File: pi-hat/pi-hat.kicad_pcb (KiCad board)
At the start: 2 copper layers, 65 x 56 mm, 67 parts, among them J1 Conn_01x04_Male, J2 Conn_01x04_Male, J3 Conn_01x05_Male, J4 Conn_01x05_Male, J5 Conn_01x05_Male, J6 Conn_01x05_Male, J7 Conn_01x07_Male, J8 Conn_01x07_Male, P1 Conn_02x20_Odd_Even, Q1 BSS138, Q10 AO 3415A, Q11 AO 3415A, Q12 BSS138, Q13 BSS138, Q14 BSS138, Q15 BSS138, Q16 BSS138, Q2 BSS138, Q3 BSS138, Q4 BC 807-25, Q5 AO 3415A, Q6 BC 807-25, Q7 BC 818-25, Q8 BC 818-25, Q9 BC 818-25, U1 M24C02-WMN

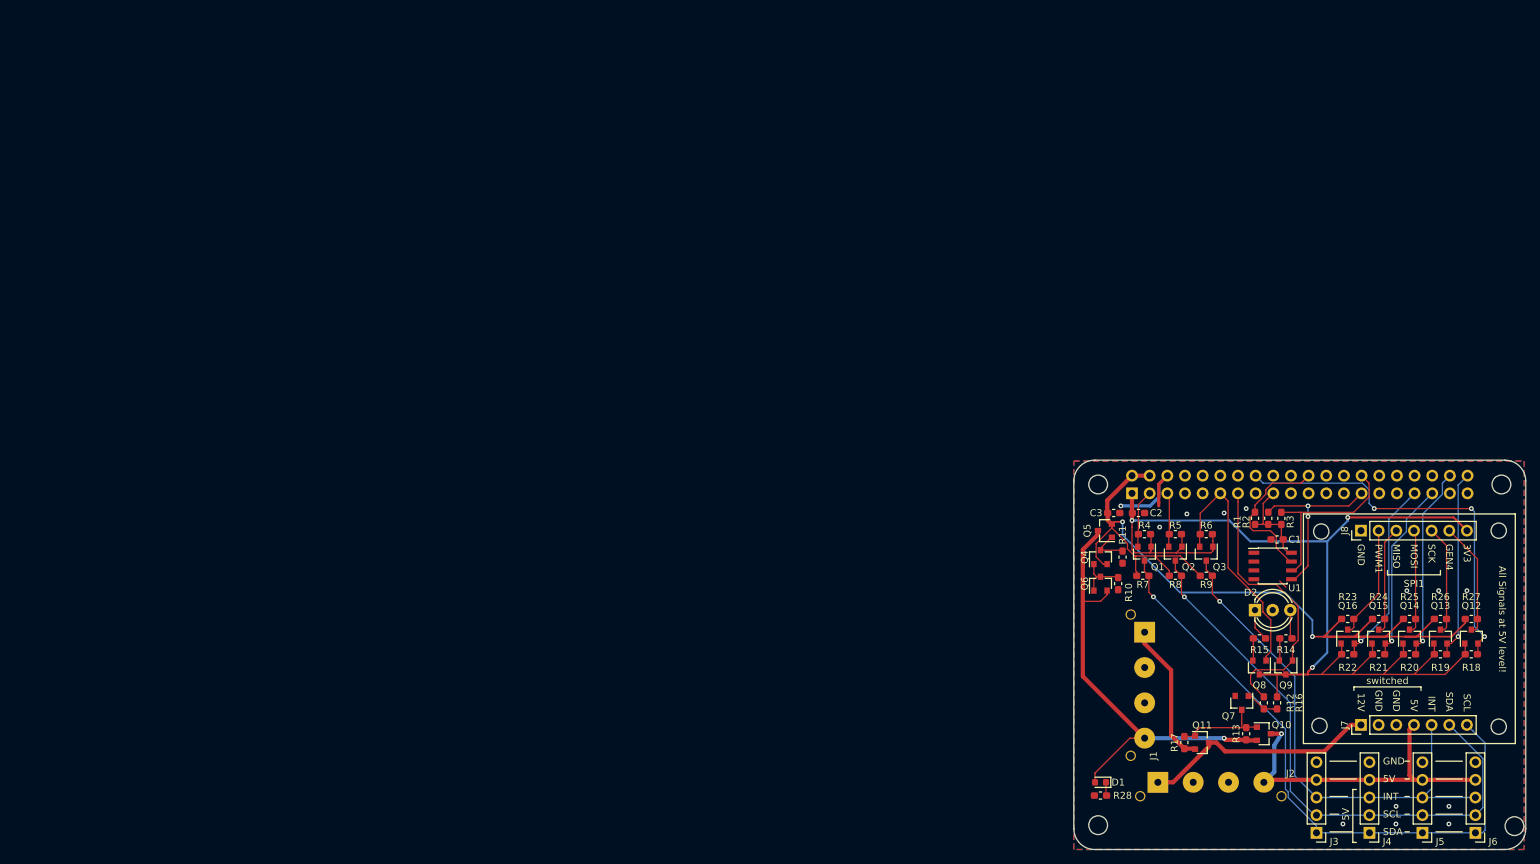
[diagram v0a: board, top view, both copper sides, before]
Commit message: PiHat: 2nd revision
* Checked and adapted MOSFET high-side switches
* remove J6 for space and fix mounting hole
* Fix Molex connectors
* Capacitors
* Extension board positions
* General layout
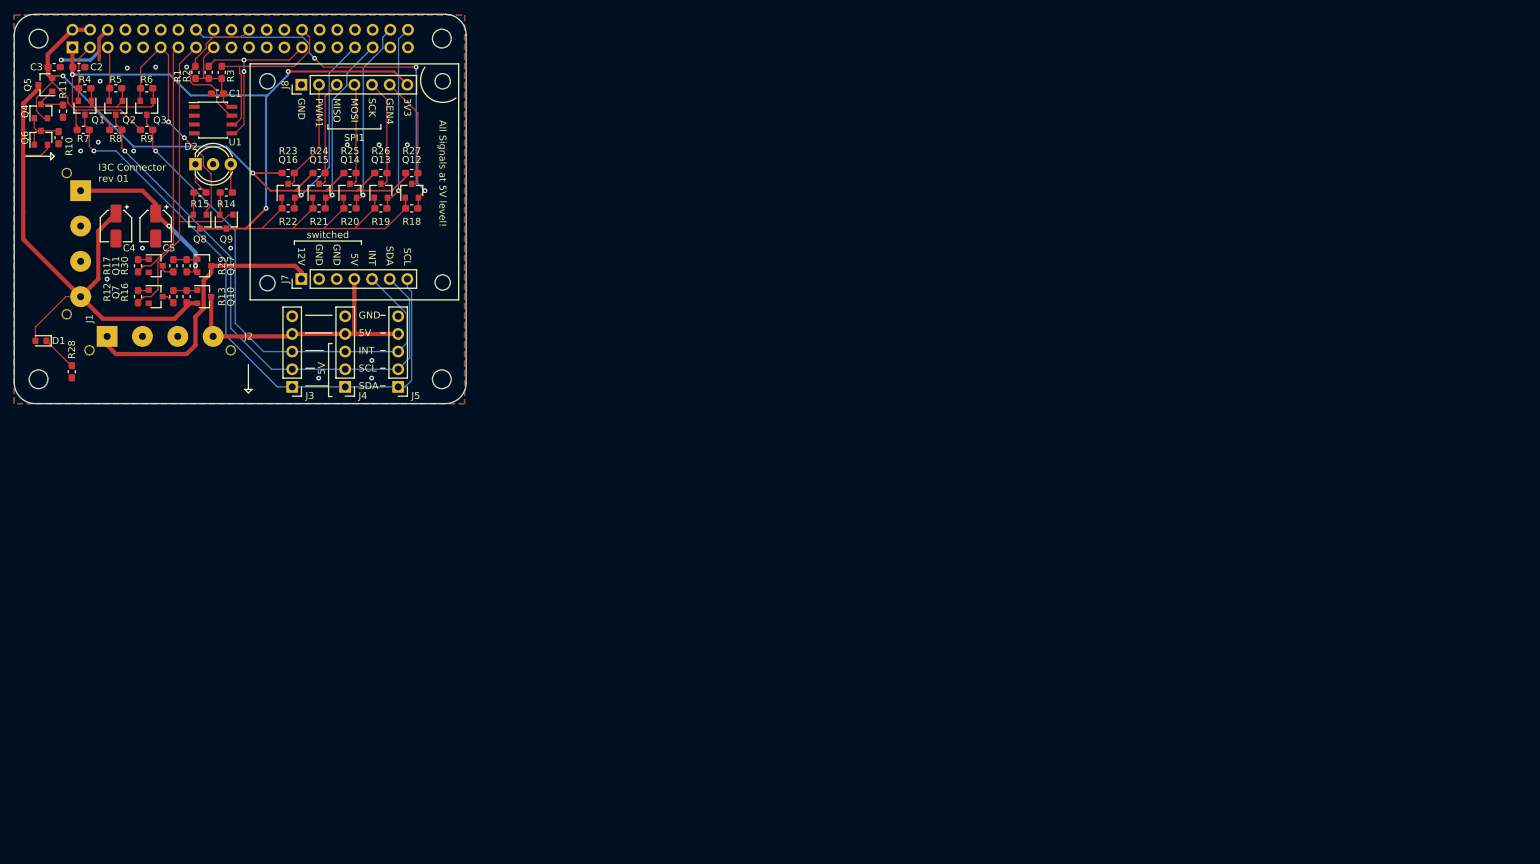
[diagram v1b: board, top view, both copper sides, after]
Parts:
- removed J6: Conn_01x05_Male, Connector_PinHeader_2.54mm:PinHeader_1x05_P2.54mm_Vertical
- added C4: 47u, Capacitor_SMD:CP_Elec_4x4.5, F.Cu at (62.2, 60.3)
- added C5: 47u, Capacitor_SMD:CP_Elec_4x4.5, F.Cu at (67.9, 60.3)
- added Q17: AO 3415A, Package_TO_SOT_SMD:SOT-23, F.Cu at (74.9, 66.0)
- added R29: 1K, Capacitor_SMD:C_0603_1608Metric_Pad1.05x0.95mm_HandSolder, F.Cu at (72.4, 66.0)
- added R30: 10R, Capacitor_SMD:C_0603_1608Metric_Pad1.05x0.95mm_HandSolder, F.Cu at (70.5, 66.0)
- Q11: value AO 3415A -> BC 818-25
- R12: value 330R -> 220R
- R16: value 1K -> 10R
- R17: value 1K -> 220R
- moved R12 172.1 mm to (65.4, 70.5), turned to 270 degrees
- moved R16 169.2 mm to (70.5, 70.5)
- moved MK4 167.1 mm to (109.1, 82.5)
- moved Q7 166.8 mm to (67.9, 70.5), turned to 0 degrees
- moved J1 165.7 mm to (57.1, 62.9)
- moved Q11 165.4 mm to (67.9, 66.0)
- moved R17 165.4 mm to (65.4, 66.0), turned to 270 degrees
- moved C1 165.3 mm to (76.8, 41.3)
- moved C3 165.3 mm to (53.3, 37.5)
- moved D2 165.3 mm to (73.7, 51.4)
- moved J7 165.3 mm to (88.9, 67.9)
- moved J8 165.3 mm to (88.9, 40.0)
- moved MK1 165.3 mm to (51.1, 33.4)
- moved MK2 165.3 mm to (109.1, 33.4)
- moved MK3 165.3 mm to (51.1, 82.4)
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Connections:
- P1 pad 13: ACTIVATE -> ACTIVATE_12V
- P1 pad 15: (no net) -> ACTIVATE_5V
- Q11 pad 1: Net-(Q10-Pad1) -> Net-(Q11-Pad1)
- Q11 pad 2: +12V -> GND
- Q11 pad 3: +12VA -> Net-(Q11-Pad3)
- Q7 pad 3: Net-(Q10-Pad1) -> Net-(Q7-Pad3)
- Q9 pad 1: ACTIVATE -> ACTIVATE_5V
- R12 pad 2: ACTIVATE -> ACTIVATE_5V
- R16 pad 1: +3V3 -> Net-(Q10-Pad1)
- R16 pad 2: Net-(Q7-Pad1) -> Net-(Q7-Pad3)
- R17 pad 1: +12V -> Net-(Q11-Pad1)
- R17 pad 2: Net-(Q10-Pad1) -> ACTIVATE_12V
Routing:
- net ACTIVATE_5V: track 0.00 -> 48.9 mm
- net ACTIVATE: track 41.2 -> 0.00 mm
- net ACTIVATE_12V: track 0.00 -> 35.3 mm
- net +5VP: track 65.7 -> 85.2 mm, vias 1 -> 0
- net +5V: track 128.6 -> 116.4 mm
- net Net-(Q10-Pad1): track 13.9 -> 3.48 mm
- net +12VA: track 34.0 -> 41.7 mm
- net +5VA: track 48.4 -> 41.7 mm, vias 1 -> 0
- net +12V: track 20.7 -> 27.2 mm, vias 0 -> 2
- net SCL_5V: track 83.5 -> 79.2 mm
- net Net-(Q17-Pad1): track 0.00 -> 3.48 mm
- net Net-(Q7-Pad1): track 4.91 -> 1.57 mm
- net Net-(D1-Pad1): track 1.94 -> 5.14 mm
- net +3V3: track 159.9 -> 156.9 mm
- net SDA_5V: track 90.0 -> 87.0 mm
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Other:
- board text added: "I3C Connector rev 01"
- board text added: "RASPBERRY-PI 40-PIN ADDON BOARD VIEW FROM TOP NOTE: P1 SHOULD BE FITTED ON THE REVERSE OF THE BOARD"
- board text removed: "RASPBERRY-PI 40-PIN ADDON BOARD VIEW FROM TOP NOTE: P1 SHOULD BE FITTED ON THE REVERSE OF THE BOARD ADD EDGE CUTS FROM CAMERA AND DISPLAY PORTS AS REQUIRED"

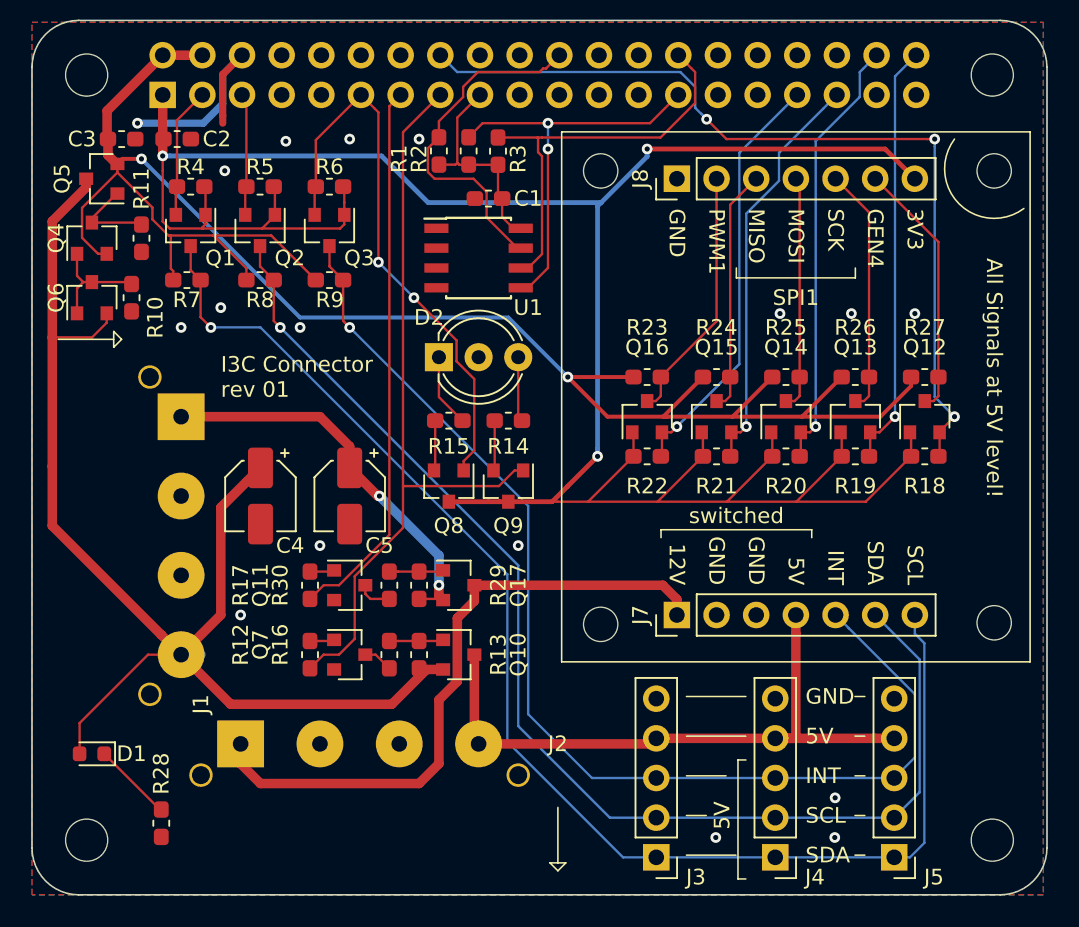
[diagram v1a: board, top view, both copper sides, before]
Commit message: Final fixes
* make sheet bigger (A3) to fix everything nicely
* fix INT LED to be low active
* fix molex holes
* fix base resistors
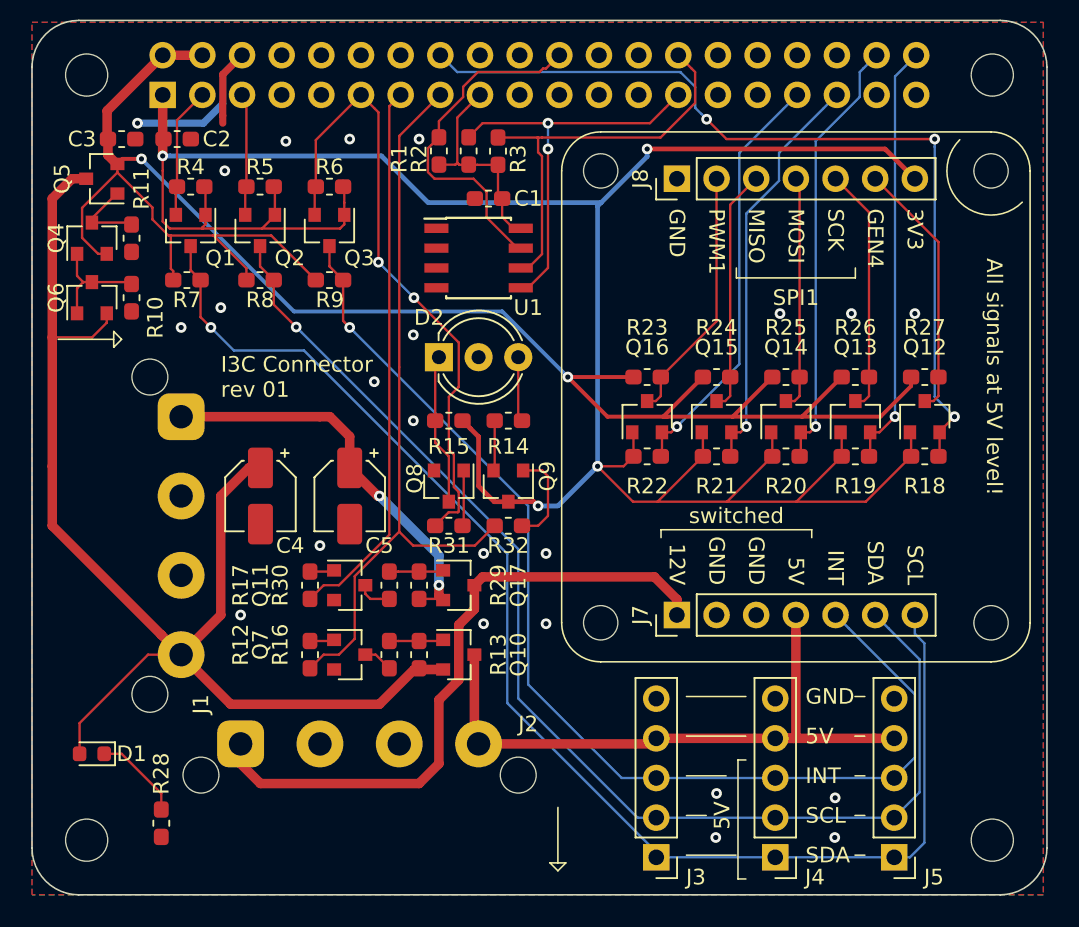
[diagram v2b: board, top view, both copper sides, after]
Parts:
- added R31: 330R, Capacitor_SMD:C_0603_1608Metric_Pad1.05x0.95mm_HandSolder, F.Cu at (74.3, 62.2)
- added R32: 330R, Capacitor_SMD:C_0603_1608Metric_Pad1.05x0.95mm_HandSolder, F.Cu at (78.1, 62.2)
- R12, R17: value 220R -> 330R
- R13, R29: value 1K -> 100K
- moved R11 0.63 mm to (54.0, 43.8)
- moved MK7 0.20 mm to (109.0, 39.5)
- moved MK8 0.20 mm to (109.0, 68.4)
- moved MK6 0.10 mm to (84.0, 68.4)
- turned R15 to 180 degrees
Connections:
- Q8 pad 1: INT -> Net-(Q8-Pad1)
- Q8 pad 2: Net-(Q8-Pad2) -> GND
- Q8 pad 3: +3V3 -> Net-(D2-Pad1)
- Q9 pad 1: ACTIVATE_5V -> Net-(Q9-Pad1)
- R15 pad 1: Net-(Q8-Pad2) -> +3V3
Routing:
- net Net-(Q9-Pad1): track 0.00 -> 6.21 mm
- net Net-(D2-Pad1): track 4.69 -> 9.72 mm
- net INT: track 36.3 -> 40.6 mm
- net Net-(Q8-Pad1): track 0.00 -> 3.57 mm
- net Net-(Q8-Pad2): track 3.22 -> 0.00 mm
- net +12V: track 27.2 -> 25.9 mm
- net INT_5V: track 73.5 -> 72.4 mm
- net ACTIVATE_5V: track 48.9 -> 47.8 mm
- net SCL_5V: track 79.2 -> 78.2 mm
- net Net-(Q4-Pad3): track 5.79 -> 5.16 mm
- net Net-(D1-Pad1): track 5.14 -> 5.74 mm
- net +3V3: track 156.9 -> 157.1 mm, vias 3 -> 4
- net GND: vias 17 -> 23
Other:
- board text added: "All signals at 5V level!"
- board text removed: "All Signals at 5V level!"

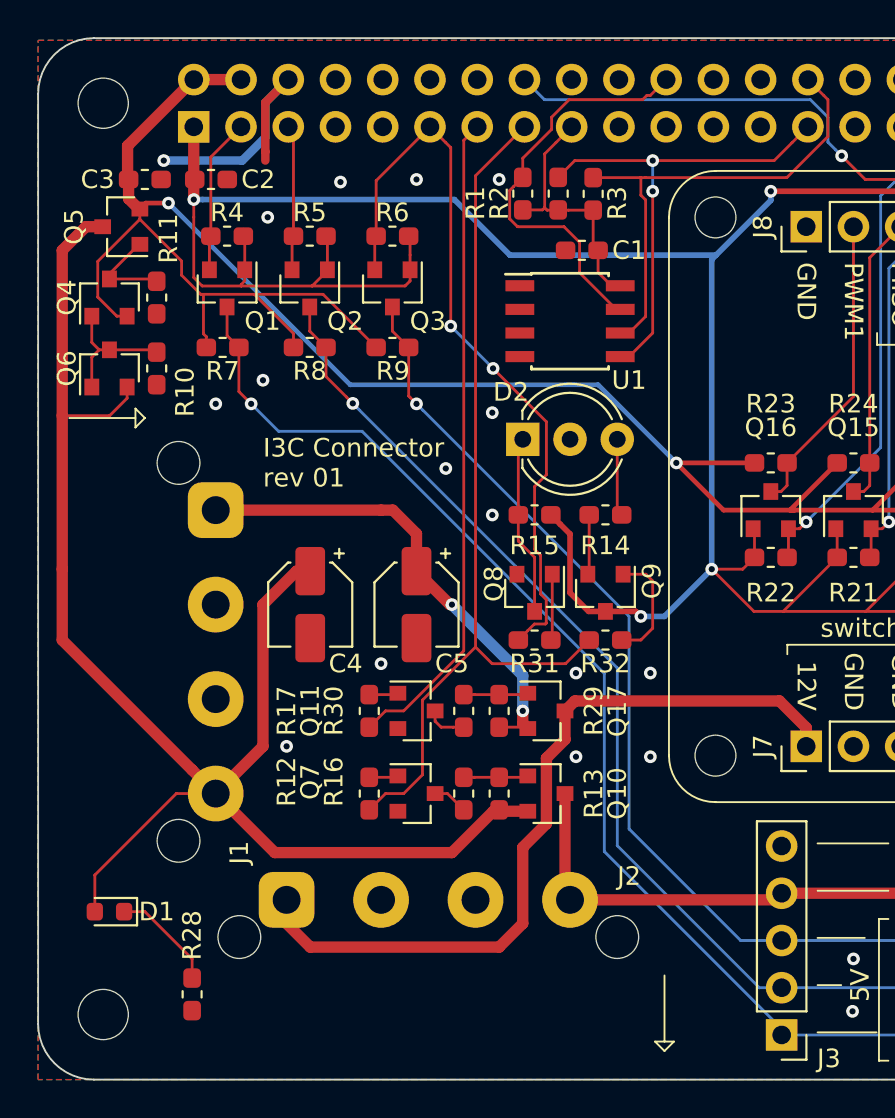
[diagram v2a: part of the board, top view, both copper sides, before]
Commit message: Add matching resistors to I3C lines
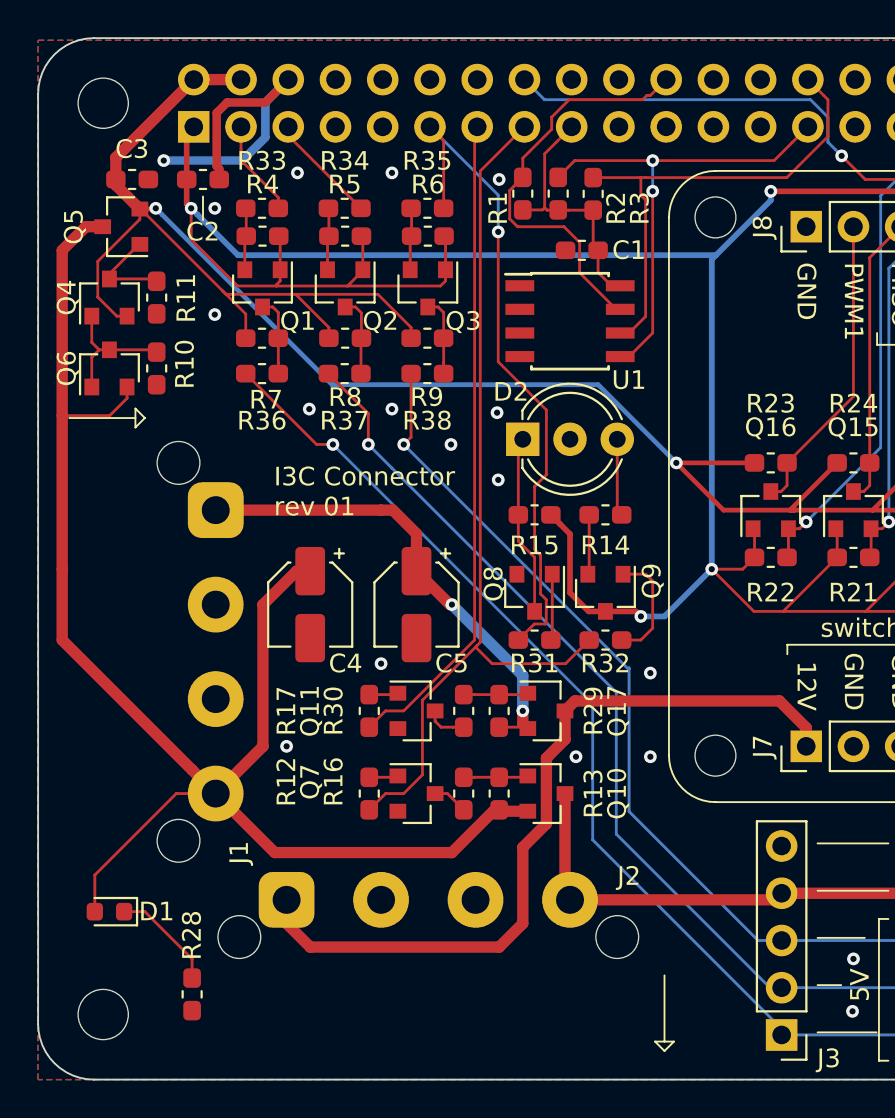
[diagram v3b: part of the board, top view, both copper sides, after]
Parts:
- added R33: 10R, Capacitor_SMD:C_0603_1608Metric_Pad1.05x0.95mm_HandSolder, F.Cu at (59.6, 39.0)
- added R34: 10R, Capacitor_SMD:C_0603_1608Metric_Pad1.05x0.95mm_HandSolder, F.Cu at (64.1, 39.0)
- added R35: 10R, Capacitor_SMD:C_0603_1608Metric_Pad1.05x0.95mm_HandSolder, F.Cu at (68.5, 39.0)
- added R36: 10R, Capacitor_SMD:C_0603_1608Metric_Pad1.05x0.95mm_HandSolder, F.Cu at (59.6, 47.9)
- added R37: 10R, Capacitor_SMD:C_0603_1608Metric_Pad1.05x0.95mm_HandSolder, F.Cu at (64.1, 47.9)
- added R38: 10R, Capacitor_SMD:C_0603_1608Metric_Pad1.05x0.95mm_HandSolder, F.Cu at (68.5, 47.9)
- R1: value 1K -> 10K
- R13, R29: value 100K -> 10K
- moved R7 2.18 mm to (59.6, 46.0)
- moved R8 1.97 mm to (64.1, 46.0)
- moved R9 1.94 mm to (68.5, 46.0)
- moved Q1 1.91 mm to (59.7, 43.3)
- moved Q2 1.91 mm to (64.1, 43.3)
- moved Q3 1.91 mm to (68.6, 43.3)
- moved R4 1.91 mm to (59.7, 40.5)
- moved R5 1.91 mm to (64.1, 40.5)
- moved R6 1.91 mm to (68.6, 40.5)
- moved C3 0.69 mm to (52.7, 37.5)
- moved C2 0.43 mm to (56.5, 37.5)
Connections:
- Q1 pad 2: SDA -> Net-(Q1-Pad2)
- Q1 pad 3: SDA_5V -> Net-(Q1-Pad3)
- Q2 pad 2: SCL -> Net-(Q2-Pad2)
- Q2 pad 3: SCL_5V -> Net-(Q2-Pad3)
- Q3 pad 2: INT -> Net-(Q3-Pad2)
- Q3 pad 3: INT_5V -> Net-(Q3-Pad3)
- R4 pad 2: SDA -> Net-(Q1-Pad2)
- R5 pad 2: SCL -> Net-(Q2-Pad2)
- R6 pad 2: INT -> Net-(Q3-Pad2)
- R7 pad 2: SDA_5V -> Net-(Q1-Pad3)
- R8 pad 2: SCL_5V -> Net-(Q2-Pad3)
- R9 pad 2: INT_5V -> Net-(Q3-Pad3)
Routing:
- net SDA_5V: track 86.5 -> 80.4 mm
- net SCL_5V: track 78.2 -> 73.9 mm
- net Net-(Q2-Pad3): track 0.00 -> 4.28 mm
- net Net-(Q1-Pad3): track 0.00 -> 4.26 mm
- net Net-(Q3-Pad3): track 0.00 -> 4.26 mm
- net INT: track 40.6 -> 36.4 mm, vias 2 -> 1
- net INT_5V: track 72.4 -> 68.2 mm
- net Net-(Q3-Pad2): track 0.00 -> 3.71 mm
- net Net-(Q1-Pad2): track 0.00 -> 3.71 mm
- net Net-(Q2-Pad2): track 0.00 -> 3.61 mm
- net GND: track 14.5 -> 17.8 mm
- net SDA: track 8.39 -> 5.21 mm
- net SCL: track 7.83 -> 6.00 mm
- net +5V: track 116.4 -> 117.6 mm
- net +3V3: track 157.1 -> 158.1 mm
